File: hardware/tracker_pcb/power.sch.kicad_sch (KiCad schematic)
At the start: 12 parts, among them U3 TPS62933FDRLR

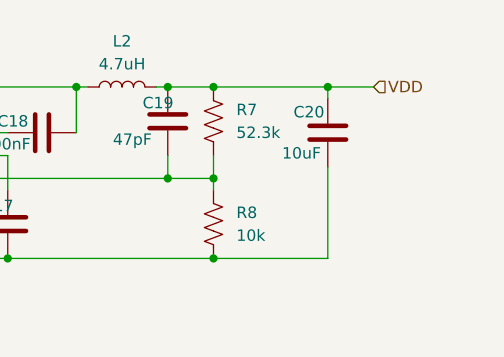
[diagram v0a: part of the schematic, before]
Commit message: More layout - adding rs485 an dinputmsheets
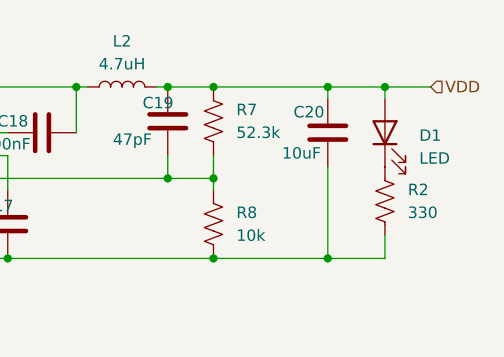
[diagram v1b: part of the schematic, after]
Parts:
- added D1: LED, LED_SMD:LED_0603_1608Metric, symbol Device:LED
- added R2: 330, Resistor_SMD:R_0603_1608Metric, symbol Device:R_US
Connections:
- net GND: now also R2.1
- net VDD: now also D1.2 (A)
- new net: D1.1 (K), R2.2
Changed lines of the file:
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@@
 	(paper "A4")
 	(junction
+		(at 194.31 106.68)
+		(diameter 0)
+		(color 0 0 0 0)
+	)
+	(junction
 		(at 181.61 87.63)
 		(diameter 0)
@@
 	)
 	(junction
+		(at 200.66 87.63)
+		(diameter 0)
+		(color 0 0 0 0)
+	)
+	(junction
 		(at 96.52 87.63)
 		(diameter 0)
@@
 	(wire
 		(pts
+			(xy 200.66 87.63) (xy 205.74 87.63)
+		)
+		(stroke
+			(width 0)
+			(type default)
+		)
+	)
+	(wire
+		(pts
 			(xy 176.53 97.79) (xy 176.53 95.25)
 		)
@@
 	(wire
 		(pts
+			(xy 200.66 104.14) (xy 200.66 106.68)
+		)
+		(stroke
+			(width 0)
+			(type default)
+		)
+	)
+	(wire
+		(pts
 			(xy 181.61 97.79) (xy 181.61 99.06)
 		)
@@
 	(wire
 		(pts
+			(xy 200.66 106.68) (xy 194.31 106.68)
+		)
+		(stroke
+			(width 0)
+			(type default)
+		)
+	)
+	(wire
+		(pts
 			(xy 111.76 106.68) (xy 111.76 101.6)
 		)
@@
 	(wire
 		(pts
-			(xy 194.31 87.63) (xy 199.39 87.63)
+			(xy 194.31 87.63) (xy 200.66 87.63)
 		)
 		(stroke
@@
 		(pts
 			(xy 176.53 87.63) (xy 175.26 87.63)
+		)
+		(stroke
+			(width 0)
+			(type default)
+		)
+	)
+	(wire
+		(pts
+			(xy 200.66 87.63) (xy 200.66 88.9)
 		)
 		(stroke
@@
 	(hierarchical_label "VDD"
 		(shape input)
-		(at 199.39 87.63 0)
+		(at 205.74 87.63 0)
 		(effects
 			(font
@@
 				(path "/6aaa9514-f94e-4843-90d0-16960e4e49cb/4c324161-c4da-41f3-8af5-33f4b9a0442d"
 					(reference "C19")
+					(unit 1)
+				)
+			)
+		)
+	)
+	(symbol
+		(lib_id "Device:R_US")
+		(at 200.66 100.33 180)
+		(unit 1)
+		(exclude_from_sim no)
+		(in_bom yes)
+		(on_board yes)
+		(dnp no)
+		(fields_autoplaced yes)
+		(property "Reference" "R2"
+			(at 203.2 99.0599 0)
+			(effects
+				(font
+					(size 1.27 1.27)
+				)
+				(justify right)
+			)
+		)
+		(property "Value" "330"
+			(at 203.2 101.5999 0)
+			(effects
+				(font
+					(size 1.27 1.27)
+				)
+				(justify right)
+			)
+		)
+		(property "Footprint" "Resistor_SMD:R_0603_1608Metric"
+			(at 199.644 100.076 90)
+			(effects
+				(font
+					(size 1.27 1.27)
+				)
+				(hide yes)
+			)
+		)
+		(property "Datasheet" "~"
+			(at 200.66 100.33 0)
+			(effects
+				(font
+					(size 1.27 1.27)
+				)
+				(hide yes)
+			)
+		)
+		(property "Description" "Resistor, US symbol"
+			(at 200.66 100.33 0)
+			(effects
+				(font
+					(size 1.27 1.27)
+				)
+				(hide yes)
+			)
+		)
+		(pin "1"
+		)
+		(pin "2"
+		)
+		(instances
+			(project "tracker_pcb"
+				(path "/6aaa9514-f94e-4843-90d0-16960e4e49cb/4c324161-c4da-41f3-8af5-33f4b9a0442d"
+					(reference "R2")
 					(unit 1)
 				)
@@
 					(unit 1)
 				)
+			)
+		)
+	)
+	(symbol
+		(lib_id "Device:LED")
+		(at 200.66 92.71 90)
+		(unit 1)
+		(exclude_from_sim no)
+		(in_bom yes)
+		(on_board yes)
+		(dnp no)
+		(fields_autoplaced yes)
+		(property "Reference" "D1"
+			(at 204.47 93.0274 90)
+			(effects
+				(font
+					(size 1.27 1.27)
+				)
+				(justify right)
+			)
+		)
+		(property "Value" "LED"
+			(at 204.47 95.5674 90)
+			(effects
+				(font
+					(size 1.27 1.27)
+				)
+				(justify right)
+			)
+		)
+		(property "Footprint" "LED_SMD:LED_0603_1608Metric"
+			(at 200.66 92.71 0)
+			(effects
+				(font
+					(size 1.27 1.27)
+				)
+				(hide yes)
+			)
+		)
+		(property "Datasheet" "~"
+			(at 200.66 92.71 0)
+			(effects
+				(font
+					(size 1.27 1.27)
+				)
+				(hide yes)
+			)
+		)
+		(property "Description" "Light emitting diode"
+			(at 200.66 92.71 0)
+			(effects
+				(font
+					(size 1.27 1.27)
+				)
+				(hide yes)
+			)
+		)
+		(property "Sim.Pins" "1=K 2=A"
+			(at 200.66 92.71 0)
+			(effects
+				(font
+					(size 1.27 1.27)
+				)
+				(hide yes)
+			)
+		)
+		(pin "2"
+		)
+		(pin "1"
+		)
+		(instances
+			(project ""
+				(path "/6aaa9514-f94e-4843-90d0-16960e4e49cb/4c324161-c4da-41f3-8af5-33f4b9a0442d"
+					(reference "D1")
+					(unit 1)
+				)

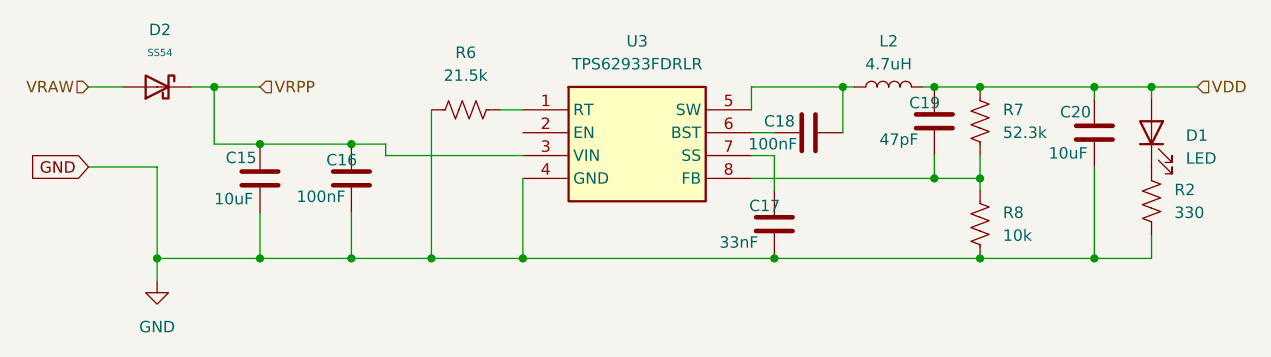
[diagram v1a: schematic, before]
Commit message: Complete but optos are using 5v pullups instead of 3v3.  No bueno
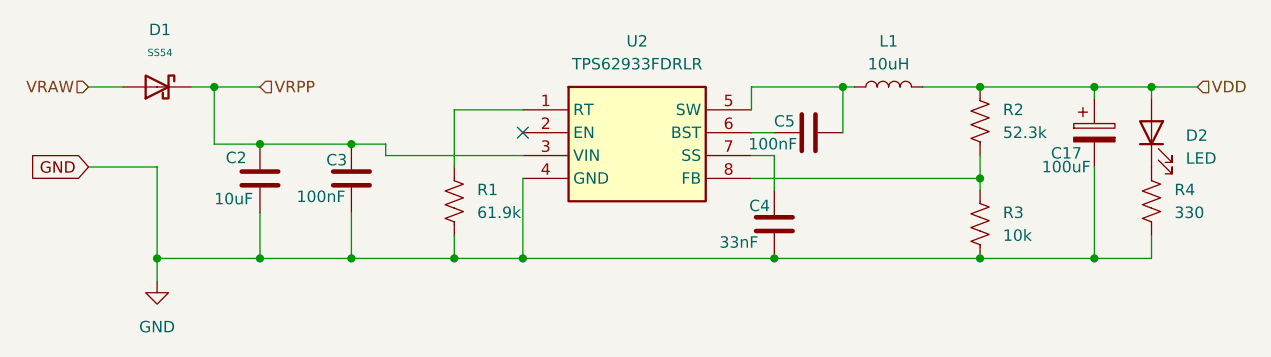
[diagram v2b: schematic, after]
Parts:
- removed C19: 47pF, Capacitor_SMD:C_0603_1608Metric, symbol Device:C
- removed C20: 10uF, Capacitor_SMD:C_0603_1608Metric, symbol Device:C
- removed R6: 21.5k, Resistor_SMD:R_0603_1608Metric, symbol Device:R_US
- added C17: 100uF, Capacitor_SMD:CP_Elec_10x10.5, symbol Device:C_Polarized
- added R1: 61.9k, Resistor_SMD:R_0603_1608Metric, symbol Device:R_US
- L1: renamed from L2; value 4.7uH -> 10uH; footprint Inductor_SMD:L_12x12mm_H6mm -> Inductor_SMD:L_Changjiang_FXL1350
- renumbered C15 to C2, C16 to C3, C17 to C4, C18 to C5, D2 to D1, D1 to D2, R7 to R2, R8 to R3, R2 to R4, U3 to U2
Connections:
- net GND: now also C17.2, R1.1
- net VDD: now also C17.1
- net at U2.1 (RT): now also R1.2
- no-connect marks 0 -> 1

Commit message: WIP
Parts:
- removed D1: SS54, Diode_SMD:D_SMA, symbol PCM_JLCPCB-Diodes:Schottky,SS54
- added U4: STPS30L30DJF-TR, footprint:SON_0L30DJF-TR_STM, symbol symbol:STPS30L30DJF-TR
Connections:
- net VRAW: now also U4.1, U4.2, U4.3, U4.4
- net VRPP: now also U4.5, U4.6, U4.7, U4.8

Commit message: Including LORA wio-sx1262
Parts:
- added C7, C8: 10uF, Capacitor_SMD:C_1206_3216Metric, symbol Device:C
- added C9: 100nF, Capacitor_SMD:C_0603_1608Metric, symbol Device:C
- added R2: 16.9k, Resistor_SMD:R_0603_1608Metric, symbol Device:R_US
- added R3: 5.00k, Resistor_SMD:R_0603_1608Metric, symbol Device:R_US
- added U4: TPS2117DRLR, footprint:SOTFL50P160X60-8N, symbol symbol:TPS2117DRLR
- added U5: TLV1117LV33DCYR, footprint:VREG_TLV1117LV33DCYR, symbol symbol:TLV1117LV33DCYR
- C2: LCSC (none) -> C1849
- C3, C5: LCSC (none) -> C1590
- C4: LCSC (none) -> C1614
- C6: renamed from C17; LCSC (none) -> C59944
- D2: LCSC (none) -> C12624
- L1: LCSC (none) -> C526017
- R1: LCSC (none) -> C23091
- R4: renamed from R2; LCSC (none) -> C185323
- R5: renamed from R3; LCSC (none) -> C25804
- R6: renamed from R4; LCSC (none) -> C23138
- U3: renamed from U2; LCSC (none) -> C5219272
- renumbered U4 to U2
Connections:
- net GND: now also C7.2, C8.2, C9.2, R3.1, U4.1 (GND), U5.1 (GND)
- net VDD: now also C7.1, U4.2 (VOUT), U4.7 (VOUT__1), U5.3 (IN); no longer C6.1, L1.2, R4.2
- net VRAW: now also U2.A; no longer U2.1, U2.2, U2.3, U2.4
- net VRPP: now also U2.K; no longer U2.5, U2.6, U2.7, U2.8
- new net: R2.1, R3.2, U4.4 (PR1)
- new net: C6.1, L1.2, R4.2, U4.6 (VIN2)
- new net V33: C8.1, C9.1, U5.2 (OUT_2), U5.4 (OUT_4)
- new net VBUS: R2.2, U4.3 (VIN1), U4.5 (MODE)
- no-connect marks 1 -> 2
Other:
- moved on the sheet: D2, R6

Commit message: VIA changes
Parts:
- R2: LCSC (none) -> C25954
- R3: value 5.00k -> 5.1k; LCSC (none) -> C23186
- U2: LCSC (none) -> C501055
- U4: LCSC (none) -> C22399676
- U5: LCSC (none) -> C15578
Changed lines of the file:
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@@
+			)
+		)
+		(property "LCSC" "C15578"
+			(at 215.5825 26.67 0)
+			(effects
+				(font
+					(size 1.27 1.27)
+				)
+				(hide yes)
 			)
 		)
@@
 			)
 		)
+		(property "LCSC" "C25954"
+			(at 130.81 31.7499 0)
+			(effects
+				(font
+					(size 1.27 1.27)
+				)
+				(hide yes)
+			)
+		)
 		(pin "1"
 		)
@@
 			)
 		)
-		(property "Value" "5.00k"
+		(property "Value" "5.1k"
 			(at 130.81 44.4499 0)
 			(effects
@@
 		(property "Description" "Resistor, US symbol"
 			(at 128.27 43.18 0)
+			(effects
+				(font
+					(size 1.27 1.27)
+				)
+				(hide yes)
+			)
+		)
+		(property "LCSC" "C23186"
+			(at 130.81 41.9099 0)
 			(effects
 				(font
@@
 			)
 		)
+		(property "LCSC" "C22399676"
+			(at 167.64 21.59 0)
+			(effects
+				(font
+					(size 1.27 1.27)
+				)
+				(hide yes)
+			)
+		)
 		(pin "4"
 		)
@@
 			(effects
 				(font
+					(size 1.27 1.27)
+				)
+				(hide yes)
+			)
+		)
+		(property "LCSC" "C501055"
+			(at 81.915 80.01 0)
+			(effects
+				(font

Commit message: wip
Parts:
- removed U2: STPS30L30DJF-TR, footprint:SON_0L30DJF-TR_STM, symbol symbol:STPS30L30DJF-TR
- added CR1: V60D60C-M3/I, footprint:DPAK_60C-M3&slash_I_VIS, symbol symbol:V60D60C-M3_I
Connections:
- net VRAW: now also CR1.1, CR1.2
- net VRPP: now also CR1.3
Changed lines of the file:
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@@
+	)
+	(junction
+		(at 72.39 87.63)
+		(diameter 0)
+		(color 0 0 0 0)
 	)
 	(junction
@@
 	(wire
 		(pts
-			(xy 82.55 96.52) (xy 90.17 96.52)
+			(xy 82.55 106.68) (xy 90.17 106.68)
 		)
 		(stroke
@@
 	(wire
 		(pts
+			(xy 62.23 87.63) (xy 72.39 87.63)
+		)
+		(stroke
+			(width 0)
+			(type default)
+		)
+	)
+	(wire
+		(pts
 			(xy 182.88 29.21) (xy 191.77 29.21)
 		)
@@
 	(wire
 		(pts
+			(xy 72.39 82.55) (xy 72.39 87.63)
+		)
+		(stroke
+			(width 0)
+			(type default)
+		)
+	)
+	(wire
+		(pts
 			(xy 236.22 43.18) (xy 236.22 46.99)
 		)
@@
 	(wire
 		(pts
-			(xy 62.23 87.63) (xy 78.74 87.63)
-		)
-		(stroke
-			(width 0)
-			(type default)
-		)
-	)
-	(wire
-		(pts
 			(xy 130.81 97.79) (xy 130.81 106.68)
 		)
@@
 	(wire
 		(pts
+			(xy 72.39 87.63) (xy 72.39 92.71)
+		)
+		(stroke
+			(width 0)
+			(type default)
+		)
+	)
+	(wire
+		(pts
 			(xy 90.17 67.31) (xy 128.27 67.31)
 		)
@@
 		(pts
 			(xy 231.14 43.18) (xy 231.14 46.99)
-		)
-		(stroke
-			(width 0)
-			(type default)
-		)
-	)
-	(wire
-		(pts
-			(xy 90.17 96.52) (xy 90.17 106.68)
 		)
 		(stroke
@@
 	(global_label "GND"
 		(shape input)
-		(at 82.55 96.52 180)
+		(at 82.55 106.68 180)
 		(fields_autoplaced yes)
 		(effects
@@
 		)
 		(property "Intersheetrefs" "${INTERSHEET_REFS}"
-			(at 75.6943 96.52 0)
+			(at 75.6943 106.68 0)
 			(effects
 				(font
@@
 			)
 		)
-		(property "Datasheet" ""
+		(property "Datasheet" "https://www.ti.com/lit/ds/symlink/tps2117.pdf?ts=1768062676098&ref_url=https%253A%252F%252Fwww.ti.com%252Fproduct%252FTPS2117%252Fpart-details%252FTPS2117DRLR%253Futm_source%253Dgoogle%2526utm_medium%253Dcpc%2526utm_campaign%253Dapp-null-null-app_opn_en-cpc-storeic-google-ww_en_pur%2526utm_content%253DDevice%2526ds_k%253DTPS2117DRLR%2526DCM%253Dyes%2526gclsrc%253Daw.ds%2526gad_source%253D1%2526gad_campaignid%253D18950597671%2526gbraid%253D0AAAAAC068F3NAfpLrBYv5TVkBwdQ7VKTc%2526gclid%253DCjwKCAiAjojLBhAlEiwAcjhrDoGEAmqFiV8xqXebAUJoi0uhbEGXIRQUOlSnADgKFNQGyquWk8rHzBoCddYQAvD_BwE"
 			(at 167.64 36.83 0)
 			(effects
@@
 	)
 	(symbol
-		(lib_id "symbol:STPS30L30DJF-TR")
-		(at 64.77 82.55 0)
+		(lib_id "symbol:V60D60C-M3_I")
+		(at 54.61 82.55 0)
 		(unit 1)
 		(exclude_from_sim no)
@@
 		(dnp no)
 		(fields_autoplaced yes)
-		(property "Reference" "U2"
-			(at 81.915 80.01 0)
+		(property "Reference" "CR1"
+			(at 79.375 74.93 0)
 			(effects
 				(font
@@
 			)
 		)
-		(property "Value" "STPS30L30DJF-TR"
-			(at 81.915 82.55 0)
+		(property "Value" "V60D60C-M3/I"
+			(at 79.375 77.47 0)
 			(effects
 				(font
@@
 			)
 		)
-		(property "Footprint" "footprint:SON_0L30DJF-TR_STM"
-			(at 66.548 76.454 0)
+		(property "Footprint" "footprint:DPAK_60C-M3&slash_I_VIS"
+			(at 68.072 77.978 0)
 			(effects
 				(font
@@
 			)
 		)
-		(property "Datasheet" ""
-			(at 64.77 82.55 0)
+		(property "Datasheet" "https://www.vishay.com/doc?87554"
+			(at 68.326 86.868 0)
 			(effects
 				(font
@@
 		)
 		(property "Description" ""
-			(at 64.77 82.55 0)
-			(effects
-				(font
-					(size 1.27 1.27)
-				)
-				(hide yes)
-			)
-		)
-		(property "LCSC" "C501055"
-			(at 81.915 80.01 0)
-			(effects
-				(font
-					(size 1.27 1.27)
-				)
-				(hide yes)
-			)
-		)
-		(pin "K"
-		)
-		(pin "A"
+			(at 54.61 82.55 0)
+			(effects
+				(font
+					(size 1.27 1.27)
+				)
+				(hide yes)
+			)
+		)
+		(pin "2"
+		)
+		(pin "3"
+		)
+		(pin "1"
 		)
 		(instances
 			(project ""
 				(path "/6aaa9514-f94e-4843-90d0-16960e4e49cb/4c324161-c4da-41f3-8af5-33f4b9a0442d"
-					(reference "U2")
+					(reference "CR1")
 					(unit 1)
 				)

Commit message: ss changes
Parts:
- CR1: LCSC (none) -> C3759778
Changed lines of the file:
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@@
+			)
+		)
+		(property "LCSC" "C3759778"
+			(at 79.375 74.93 0)
+			(effects
+				(font
+					(size 1.27 1.27)
+				)
+				(hide yes)
 			)
 		)

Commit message: Add fuseholder
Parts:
- added F1: 3557-2, footprint:FUSE_3557-2, symbol symbol:3557-2
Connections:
- net VRAW: now also F1.1_1, F1.1_2; no longer CR1.1, CR1.2
- new net: CR1.1, CR1.2, F1.2_1, F1.2_2
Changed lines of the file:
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@@
 	(wire
 		(pts
-			(xy 62.23 87.63) (xy 72.39 87.63)
+			(xy 49.53 87.63) (xy 52.07 87.63)
 		)
 		(stroke
@@
 		(pts
 			(xy 215.9 46.99) (xy 204.47 46.99)
+		)
+		(stroke
+			(width 0)
+			(type default)
+		)
+	)
+	(wire
+		(pts
+			(xy 67.31 87.63) (xy 72.39 87.63)
 		)
 		(stroke
@@
 	(hierarchical_label "VRAW"
 		(shape input)
-		(at 62.23 87.63 180)
+		(at 49.53 87.63 180)
 		(effects
 			(font
@@
 					(unit 1)
 				)
+			)
+		)
+	)
+	(symbol
+		(lib_id "symbol:3557-2")
+		(at 59.69 87.63 0)
+		(unit 1)
+		(exclude_from_sim no)
+		(in_bom yes)
+		(on_board yes)
+		(dnp no)
+		(property "Reference" "F1"
+			(at 59.69 81.28 0)
+			(effects
+				(font
+					(size 1.27 1.27)
+				)
+			)
+		)
+		(property "Value" "3557-2"
+			(at 59.436 84.328 0)
+			(effects
+				(font
+					(size 1.27 1.27)
+				)
+			)
+		)
+		(property "Footprint" "footprint:FUSE_3557-2"
+			(at 59.69 87.63 0)
+			(effects
+				(font
+					(size 1.27 1.27)
+				)
+				(justify bottom)
+				(hide yes)
+			)
+		)
+		(property "Datasheet" ""
+			(at 59.69 87.63 0)
+			(effects
+				(font
+					(size 1.27 1.27)
+				)
+				(hide yes)
+			)
+		)
+		(property "Description" ""
+			(at 59.69 87.63 0)
+			(effects
+				(font
+					(size 1.27 1.27)
+				)
+				(hide yes)
+			)
+		)
+		(property "PARTREV" "D"
+			(at 59.69 87.63 0)
+			(effects
+				(font
+					(size 1.27 1.27)
+				)
+				(justify bottom)
+				(hide yes)
+			)
+		)
+		(property "STANDARD" "Manufacturer Recommendation"
+			(at 59.69 87.63 0)
+			(effects
+				(font
+					(size 1.27 1.27)
+				)
+				(justify bottom)
+				(hide yes)
+			)
+		)
+		(property "SNAPEDA_PN" "3557-2"
+			(at 59.69 87.63 0)
+			(effects
+				(font
+					(size 1.27 1.27)
+				)
+				(justify bottom)
+				(hide yes)
+			)
+		)
+		(property "MAXIMUM_PACKAGE_HEIGHT" "7.37mm"
+			(at 59.69 87.63 0)
+			(effects
+				(font
+					(size 1.27 1.27)
+				)
+				(justify bottom)
+				(hide yes)
+			)
+		)
+		(property "MANUFACTURER" "Keystone"
+			(at 59.69 87.63 0)
+			(effects
+				(font
+					(size 1.27 1.27)
+				)
+				(justify bottom)
+				(hide yes)
+			)
+		)
+		(pin "1_2"
+		)
+		(pin "2_1"
+		)
+		(pin "1_1"
+		)
+		(pin "2_2"
+		)
+		(instances
+			(project ""
+				(path "/6aaa9514-f94e-4843-90d0-16960e4e49cb/4c324161-c4da-41f3-8af5-33f4b9a0442d"
+					(reference "F1")
+					(unit 1)
+				)
